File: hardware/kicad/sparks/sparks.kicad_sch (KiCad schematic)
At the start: 39 parts, among them J1 Conn_02x04_Odd_Even, J2 TP4056 Breakout, SW1 SW_Push, U1 MAX7219, U2 ESP32-C3-SuperMini

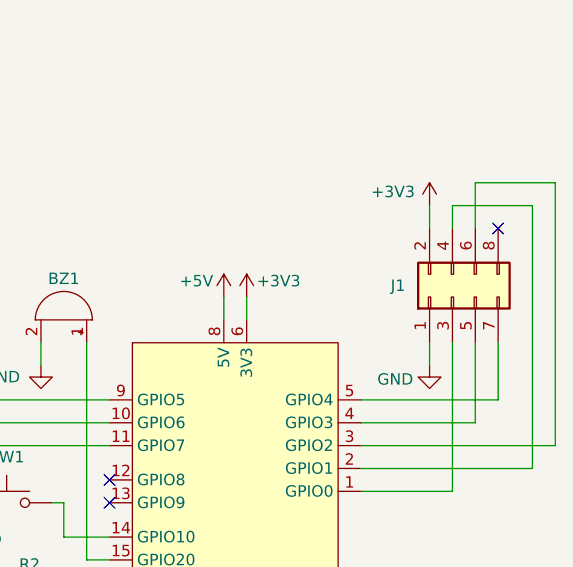
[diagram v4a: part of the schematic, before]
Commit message: Use a stock pin header for the CC1101 socket, and route DIG0
Replace the CC1101 connector with the stock
PinHeader_2x04_P2.54mm_Vertical at 90 degrees, which gives the
module's own pin arrangement directly: the top row, away from the
board, is 2 4 6 8 and the bottom row, against the board, is
1 3 5 7, with pin 1 on GND and pin 2 on 3V3.

Drop the custom footprint added earlier. It was built on the
assumption that no rotation of a stock part could produce this
layout, which came from testing rotations of the socket footprint
rather than the header - the two number their pads differently.

Route the first track: D1 to D2 on DIG0, 0.4 mm on the front
layer, 9 mm of copper over three segments. The rest of that net
still needs a via down to the MAX7219 on the back.
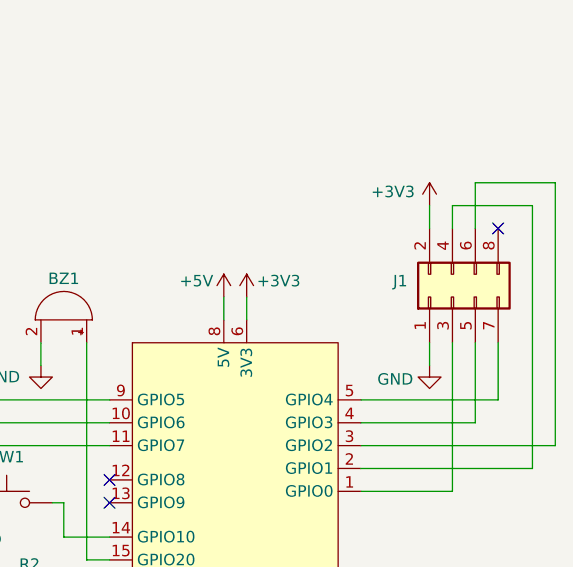
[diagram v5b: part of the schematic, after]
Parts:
- J1: footprint Sparks:CC1101_Socket_2x04 -> Connector_PinHeader_2.54mm:PinHeader_2x04_P2.54mm_Vertical
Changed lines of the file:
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@@
+	)
+	(symbol
+		(lib_id "Connector_Generic:Conn_02x04_Odd_Even")
+		(at 196.85 59.69 90)
+		(unit 1)
+		(body_style 1)
+		(exclude_from_sim no)
+		(in_bom yes)
+		(on_board yes)
+		(in_pos_files yes)
+		(dnp no)
+		(property "Reference" "J1"
+			(at 190.246 57.912 90)
+			(show_name no)
+			(do_not_autoplace no)
+			(effects
+				(font
+					(size 1.27 1.27)
+				)
+				(justify right)
+			)
+		)
+		(property "Value" "Conn_02x04_Odd_Even"
+			(at 204.47 59.6899 90)
+			(hide yes)
+			(show_name no)
+			(do_not_autoplace no)
+			(effects
+				(font
+					(size 1.27 1.27)
+				)
+				(justify right)
+			)
+		)
+		(property "Footprint" "Connector_PinHeader_2.54mm:PinHeader_2x04_P2.54mm_Vertical"
+			(at 196.85 59.69 0)
+			(hide yes)
+			(show_name no)
+			(do_not_autoplace no)
+			(effects
+				(font
+					(size 1.27 1.27)
+				)
+			)
+		)
+		(property "Datasheet" ""
+			(at 196.85 59.69 0)
+			(hide yes)
+			(show_name no)
+			(do_not_autoplace no)
+			(effects
+				(font
+					(size 1.27 1.27)
+				)
+			)
+		)
+		(property "Description" "Generic connector, double row, 02x04, odd/even pin numbering scheme (row 1 odd numbers, row 2 even numbers), script generated (kicad-library-utils/schlib/autogen/connector/)"
+			(at 196.85 59.69 0)
+			(hide yes)
+			(show_name no)
+			(do_not_autoplace no)
+			(effects
+				(font
+					(size 1.27 1.27)
+				)
+			)
+		)
+		(pin "2"
+		)
+		(pin "1"
+		)
+		(pin "5"
+		)
+		(pin "8"
+		)
+		(pin "4"
+		)
+		(pin "7"
+		)
+		(pin "3"
+		)
+		(pin "6"
+		)
+		(instances
+			(project "sparks"
+				(path "/b32579de-9b7d-4099-823e-c649101f67ab"
+					(reference "J1")
+					(unit 1)
+				)
+			)
+		)
 	)
 	(symbol
@@
 					(unit 1)
 				)
-			)
-		)
-	)
-	(symbol
-		(lib_id "Connector_Generic:Conn_02x04_Odd_Even")
-		(at 196.85 59.69 90)
-		(unit 1)
-		(body_style 1)
-		(exclude_from_sim no)
-		(in_bom yes)
-		(on_board yes)
-		(in_pos_files yes)
-		(dnp no)
-		(property "Reference" "J1"
-			(at 189.992 58.42 90)
-			(show_name no)
-			(do_not_autoplace no)
-			(effects
-				(font
-					(size 1.27 1.27)
-				)
-				(justify right)
-			)
-		)
-		(property "Value" "Conn_02x04_Odd_Even"
-			(at 204.47 59.6899 90)
-			(hide yes)
-			(show_name no)
-			(do_not_autoplace no)
-			(effects
-				(font
-					(size 1.27 1.27)
-				)
-				(justify right)
-			)
-		)
-		(property "Footprint" "Sparks:CC1101_Socket_2x04"
-			(at 196.85 59.69 0)
-			(hide yes)
-			(show_name no)
-			(do_not_autoplace no)
-			(effects
-				(font
-					(size 1.27 1.27)
-				)
-			)
-		)
-		(property "Datasheet" ""
-			(at 196.85 59.69 0)
-			(hide yes)
-			(show_name no)
-			(do_not_autoplace no)
-			(effects
-				(font
-					(size 1.27 1.27)
-				)
-			)
-		)
-		(property "Description" "Generic connector, double row, 02x04, odd/even pin numbering scheme (row 1 odd numbers, row 2 even numbers), script generated (kicad-library-utils/schlib/autogen/connector/)"
-			(at 196.85 59.69 0)
-			(hide yes)
-			(show_name no)
-			(do_not_autoplace no)
-			(effects
-				(font
-					(size 1.27 1.27)
-				)
-			)
-		)
-		(pin "7"
-		)
-		(pin "6"
-		)
-		(pin "8"
-		)
-		(pin "5"
-		)
-		(pin "3"
-		)
-		(pin "4"
-		)
-		(pin "2"
-		)
-		(pin "1"
-		)
-		(instances
-			(project "sparks"
-				(path "/b32579de-9b7d-4099-823e-c649101f67ab"
-					(reference "J1")
-					(unit 1)
-				)

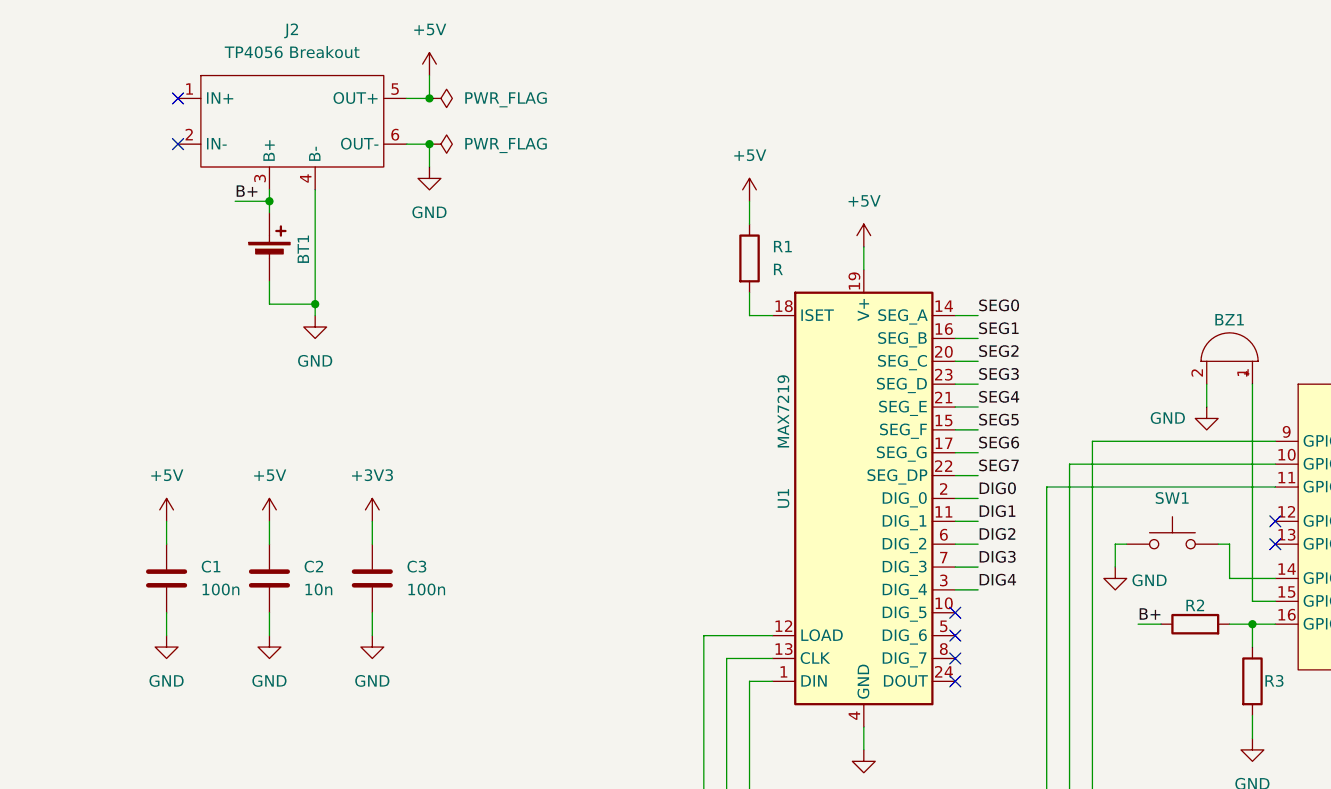
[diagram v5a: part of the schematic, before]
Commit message: Clear all routing ahead of autorouting
Remove 177 track segments and 15 vias. Placement, the ground pour,
the board outline and all 45 footprints are untouched.

Manual routing of the matrix proved impractical: the LEDs are
arranged by the Morse tree's geometry while the nets are grouped by
tree level, so same-net LEDs sit far apart and every net has to
weave through the others. Freerouting will be given the clean board
instead.

This commit is the placement-complete, unrouted state, tagged so it
can be returned to if the autorouted result is unsatisfactory.
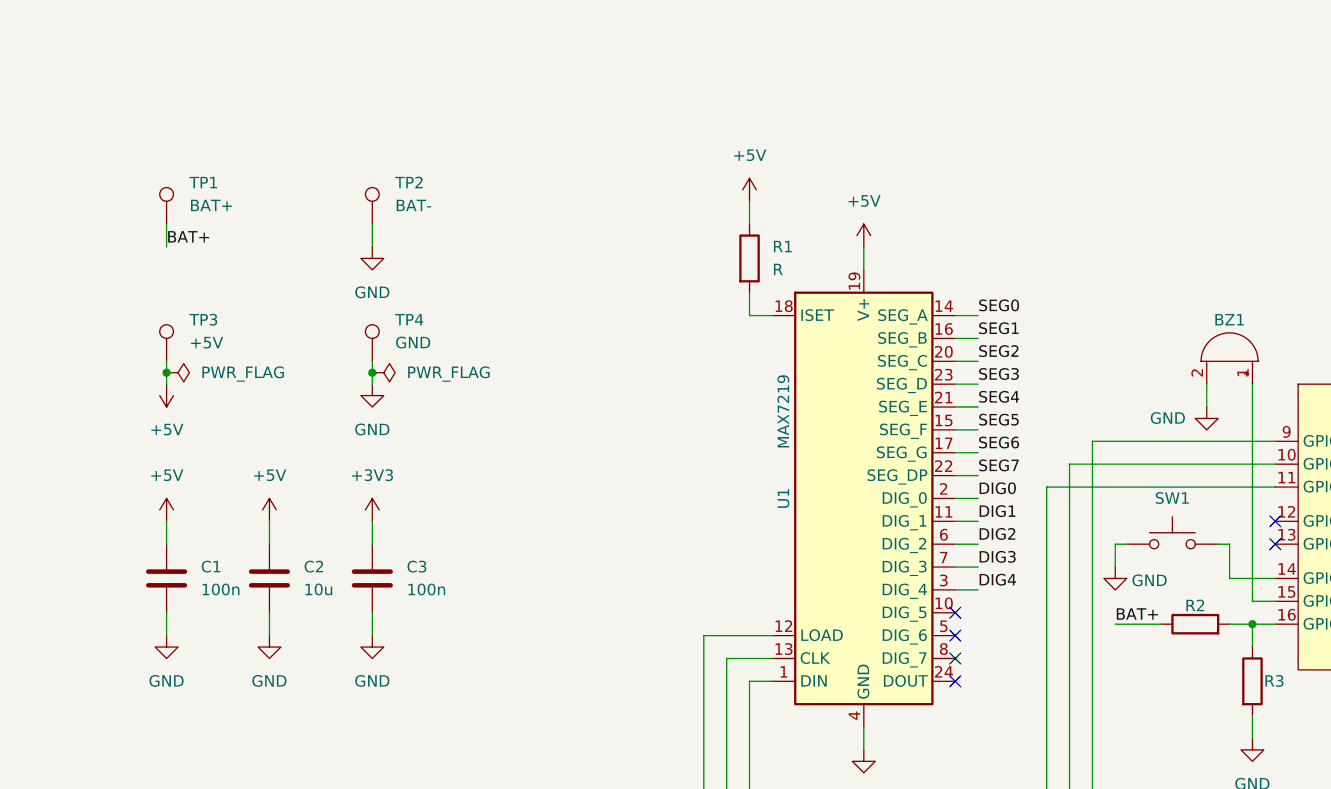
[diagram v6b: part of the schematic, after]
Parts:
- removed BT1: Battery_Cell, Connector_Wire:SolderWire-0.127sqmm_1x02_P3.7mm_D0.48mm_OD1mm_Relief, symbol Device:Battery_Cell
- removed J2: TP4056 Breakout, TP4056-Breakout:TP4056-Breakout, symbol TP4056-Breakout:TP4056_breakout
- added TP1: BAT+, TestPoint:TestPoint_THTPad_2.0x2.0mm_Drill1.0mm, symbol Connector:TestPoint
- added TP2: BAT-, TestPoint:TestPoint_THTPad_2.0x2.0mm_Drill1.0mm, symbol Connector:TestPoint
- added TP3: +5V, TestPoint:TestPoint_THTPad_2.0x2.0mm_Drill1.0mm, symbol Connector:TestPoint
- added TP4: GND, TestPoint:TestPoint_THTPad_2.0x2.0mm_Drill1.0mm, symbol Connector:TestPoint
- C2: value 10n -> 10u
- U1: footprint Package_DIP:DIP-24_W7.62mm -> Package_SO:SOIC-24W_7.5x15.4mm_P1.27mm
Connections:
- net +5V: now also TP3.1
- net GND: now also TP2.1, TP4.1
- net B+ renamed BAT+
- net BAT+: now also TP1.1
- no-connect marks 9 -> 7
